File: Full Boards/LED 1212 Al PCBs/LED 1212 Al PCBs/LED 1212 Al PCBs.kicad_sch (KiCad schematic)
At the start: 3 parts

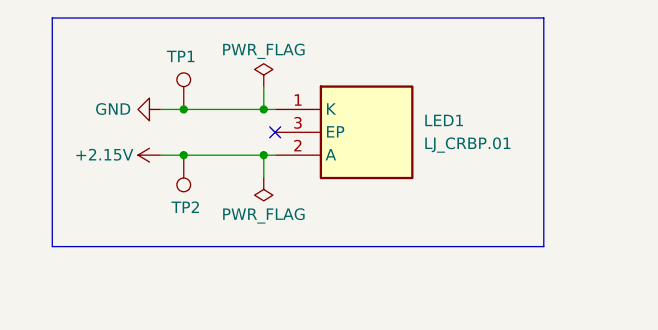
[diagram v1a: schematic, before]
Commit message: Sync'ed the USB-C PD PCB to the schematic.
Removed test points from the 1212 kicad schematic, as it was unused.

Signed-off-by: digimer <digital.mermaid@gmail.com>
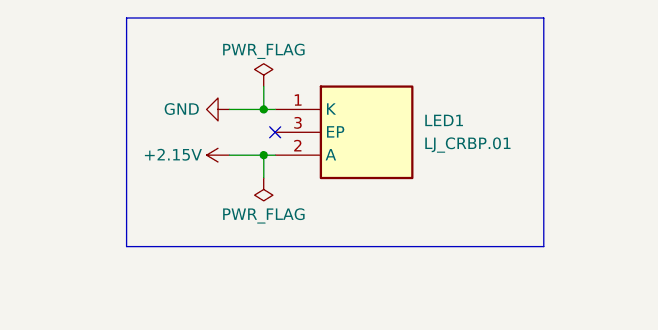
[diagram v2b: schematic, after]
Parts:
- removed TP1, TP2: TestPoint, TestPoint:TestPoint_Pad_4.0x4.0mm, symbol Connector:TestPoint
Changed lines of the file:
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@@
 	)
 	(rectangle
-		(start 92.075 72.39)
+		(start 100.33 72.39)
 		(end 146.685 97.79)
 		(stroke
@@
 	)
 	(junction
-		(at 106.68 87.63)
-		(diameter 0)
-		(color 0 0 0 0)
-	)
-	(junction
-		(at 106.68 82.55)
+		(at 115.57 87.63)
 		(diameter 0)
 		(color 0 0 0 0)
@@
 		(color 0 0 0 0)
 	)
-	(junction
-		(at 115.57 87.63)
-		(diameter 0)
-		(color 0 0 0 0)
-	)
 	(no_connect
 		(at 116.84 85.09)
@@
 	(wire
 		(pts
-			(xy 106.68 82.55) (xy 115.57 82.55)
+			(xy 111.76 82.55) (xy 115.57 82.55)
 		)
 		(stroke
@@
 	(wire
 		(pts
-			(xy 104.14 87.63) (xy 106.68 87.63)
-		)
-		(stroke
-			(width 0)
-			(type default)
-		)
-	)
-	(wire
-		(pts
-			(xy 104.14 82.55) (xy 106.68 82.55)
+			(xy 111.76 87.63) (xy 115.57 87.63)
 		)
 		(stroke
@@
 		(pts
 			(xy 115.57 82.55) (xy 116.84 82.55)
-		)
-		(stroke
-			(width 0)
-			(type default)
-		)
-	)
-	(wire
-		(pts
-			(xy 106.68 87.63) (xy 115.57 87.63)
 		)
 		(stroke
@@
 	)
 	(symbol
-		(lib_id "Connector:TestPoint")
-		(at 106.68 87.63 180)
-		(unit 1)
-		(body_style 1)
-		(exclude_from_sim no)
-		(in_bom yes)
-		(on_board yes)
-		(in_pos_files yes)
-		(dnp no)
-		(property "Reference" "TP2"
-			(at 106.934 93.472 0)
-			(show_name no)
-			(do_not_autoplace no)
-			(effects
-				(font
-					(size 1.27 1.27)
-				)
-			)
-		)
-		(property "Value" "TestPoint"
-			(at 104.14 89.6621 0)
-			(hide yes)
-			(show_name no)
-			(do_not_autoplace no)
-			(effects
-				(font
-					(size 1.27 1.27)
-				)
-				(justify left)
-			)
-		)
-		(property "Footprint" "TestPoint:TestPoint_Pad_4.0x4.0mm"
-			(at 101.6 87.63 0)
-			(hide yes)
-			(show_name no)
-			(do_not_autoplace no)
-			(effects
-				(font
-					(size 1.27 1.27)
-				)
-			)
-		)
-		(property "Datasheet" ""
-			(at 101.6 87.63 0)
-			(hide yes)
-			(show_name no)
-			(do_not_autoplace no)
-			(effects
-				(font
-					(size 1.27 1.27)
-				)
-			)
-		)
-		(property "Description" "test point"
-			(at 106.68 87.63 0)
-			(hide yes)
-			(show_name no)
-			(do_not_autoplace no)
-			(effects
-				(font
-					(size 1.27 1.27)
-				)
-			)
-		)
-		(pin "1"
-		)
-		(instances
-			(project "LED 1212 Al PCBs"
-				(path "/230f5e89-ed89-4016-bb7f-48da2e754b45"
-					(reference "TP2")
-					(unit 1)
-				)
-			)
-		)
-	)
-	(symbol
 		(lib_id "power:GND")
-		(at 104.14 82.55 270)
+		(at 111.76 82.55 270)
 		(unit 1)
 		(body_style 1)
@@
 		(dnp no)
 		(property "Reference" "#PWR02"
-			(at 97.79 82.55 0)
+			(at 105.41 82.55 0)
 			(hide yes)
 			(show_name no)
@@
 		)
 		(property "Value" "GND"
-			(at 100.838 82.55 90)
+			(at 108.458 82.55 90)
 			(show_name no)
 			(do_not_autoplace no)
@@
 		)
 		(property "Footprint" ""
-			(at 104.14 82.55 0)
+			(at 111.76 82.55 0)
 			(hide yes)
 			(show_name no)
@@
 		)
 		(property "Datasheet" ""
-			(at 104.14 82.55 0)
+			(at 111.76 82.55 0)
 			(hide yes)
 			(show_name no)
@@
 		)
 		(property "Description" "Power symbol creates a global label with name \"GND\" , ground"
-			(at 104.14 82.55 0)
+			(at 111.76 82.55 0)
 			(hide yes)
 			(show_name no)
@@
 	)
 	(symbol
-		(lib_id "Connector:TestPoint")
-		(at 106.68 82.55 0)
-		(unit 1)
-		(body_style 1)
-		(exclude_from_sim no)
-		(in_bom yes)
-		(on_board yes)
-		(in_pos_files yes)
-		(dnp no)
-		(property "Reference" "TP1"
-			(at 106.426 76.708 0)
-			(show_name no)
-			(do_not_autoplace no)
-			(effects
-				(font
-					(size 1.27 1.27)
-				)
-			)
-		)
-		(property "Value" "TestPoint"
-			(at 109.22 80.5179 0)
-			(hide yes)
-			(show_name no)
-			(do_not_autoplace no)
-			(effects
-				(font
-					(size 1.27 1.27)
-				)
-				(justify left)
-			)
-		)
-		(property "Footprint" "TestPoint:TestPoint_Pad_4.0x4.0mm"
-			(at 111.76 82.55 0)
-			(hide yes)
-			(show_name no)
-			(do_not_autoplace no)
-			(effects
-				(font
-					(size 1.27 1.27)
-				)
-			)
-		)
-		(property "Datasheet" ""
-			(at 111.76 82.55 0)
-			(hide yes)
-			(show_name no)
-			(do_not_autoplace no)
-			(effects
-				(font
-					(size 1.27 1.27)
-				)
-			)
-		)
-		(property "Description" "test point"
-			(at 106.68 82.55 0)
-			(hide yes)
-			(show_name no)
-			(do_not_autoplace no)
-			(effects
-				(font
-					(size 1.27 1.27)
-				)
-			)
-		)
-		(pin "1"
-		)
-		(instances
-			(project "LED 1212 Al PCBs"
-				(path "/230f5e89-ed89-4016-bb7f-48da2e754b45"
-					(reference "TP1")
-					(unit 1)
-				)
-			)
-		)
-	)
-	(symbol
 		(lib_id "power:+3.3V")
-		(at 104.14 87.63 90)
+		(at 111.76 87.63 90)
 		(unit 1)
 		(body_style 1)
@@
 		(dnp no)
 		(property "Reference" "#PWR01"
-			(at 107.95 87.63 0)
+			(at 115.57 87.63 0)
 			(hide yes)
 			(show_name no)
@@
 		)
 		(property "Value" "+2.15V"
-			(at 101.092 87.63 90)
+			(at 108.712 87.63 90)
 			(show_name no)
 			(do_not_autoplace no)
@@
 		)
 		(property "Footprint" ""
-			(at 104.14 87.63 0)
+			(at 111.76 87.63 0)
 			(hide yes)
 			(show_name no)
@@
 		)
 		(property "Datasheet" ""
-			(at 104.14 87.63 0)
+			(at 111.76 87.63 0)
 			(hide yes)
 			(show_name no)
@@
 		)
 		(property "Description" "Power symbol creates a global label with name \"+3.3V\""
-			(at 104.14 87.63 0)
-			(hide yes)
-			(show_name no)
+			(at 111.76 87.63 0)
+			(hide yes)
+			(show_name no)

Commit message: Updated LED 1212 PCB to add solder pads and wire solder pads (replacing what the test points were used for before).
Moved all .stp and .step files back one directory.

Signed-off-by: digimer <digital.mermaid@gmail.com>
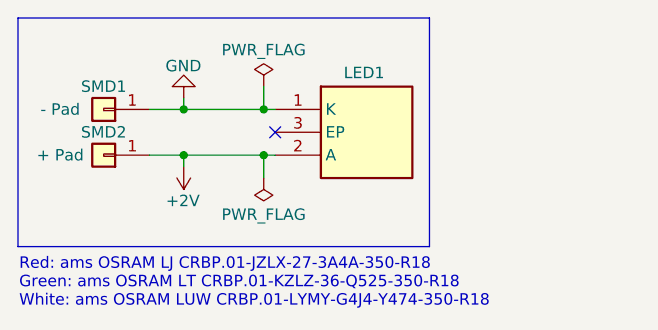
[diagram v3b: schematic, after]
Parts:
- added SMD1: - Pad, mr-stuff:SolderWirePad_1x01_SMD_4x4mm, symbol Connector_Generic:Conn_01x01
- added SMD2: + Pad, mr-stuff:SolderWirePad_1x01_SMD_4x4mm, symbol Connector_Generic:Conn_01x01
- LED1: Height 2.24 -> (none); Manufacturer_Name ams OSRAM -> (none); Manufacturer_Part_Number LJ CRBP.01-JZLX-27-3A4A -> (none); Mouser Part Number 720-LJCRBP01JZA9260 -> (none); Mouser Price/Stock https://www.mouser.co.uk/ProductDetail/ams-OSRAM/LJ-CRBP.01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 -> (none); Part - Green (none) -> ams OSRAM LT CRBP.01-KZLZ-36-Q525-350-R18; Part - Red (none) -> ams OSRAM LJ CRBP.01-JZLX-27-3A4A-350-R18; Part - White (none) -> ams OSRAM LUW CRBP.01-LYMY-G4J4-Y474-350-R18
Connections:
- net GND: now also SMD1.1 (Pin_1)
- net +2.15V renamed +2V
- net +2V: now also SMD2.1 (Pin_1)
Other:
- note added: "Red: ams OSRAM LJ CRBP.01-JZLX-27-3A4A-350-R18 Green: ams OSRAM LT CRBP.01-KZLZ-36-Q525-350-R18 White: ams OSRAM LUW CRBP.01-LYMY-G4J4-Y474-350-R18"
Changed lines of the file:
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@@
 	)
 	(rectangle
-		(start 100.33 72.39)
-		(end 146.685 97.79)
+		(start 88.265 72.39)
+		(end 133.985 97.79)
 		(stroke
 			(width 0)
@@
 		(fill
 			(type none)
+		)
+	)
+	(text "Red: ams OSRAM LJ CRBP.01-JZLX-27-3A4A-350-R18\nGreen: ams OSRAM LT CRBP.01-KZLZ-36-Q525-350-R18\nWhite: ams OSRAM LUW CRBP.01-LYMY-G4J4-Y474-350-R18"
+		(exclude_from_sim no)
+		(at 88.392 101.854 0)
+		(effects
+			(font
+				(size 1.27 1.27)
+			)
+			(justify left)
 		)
 	)
@@
 	)
 	(junction
+		(at 106.68 87.63)
+		(diameter 0)
+		(color 0 0 0 0)
+	)
+	(junction
+		(at 106.68 82.55)
+		(diameter 0)
+		(color 0 0 0 0)
+	)
+	(junction
 		(at 115.57 82.55)
 		(diameter 0)
@@
 	(wire
 		(pts
+			(xy 106.68 82.55) (xy 106.68 81.28)
+		)
+		(stroke
+			(width 0)
+			(type default)
+		)
+	)
+	(wire
+		(pts
 			(xy 115.57 87.63) (xy 115.57 90.17)
 		)
@@
 	(wire
 		(pts
+			(xy 102.87 82.55) (xy 106.68 82.55)
+		)
+		(stroke
+			(width 0)
+			(type default)
+		)
+	)
+	(wire
+		(pts
+			(xy 106.68 87.63) (xy 106.68 88.9)
+		)
+		(stroke
+			(width 0)
+			(type default)
+		)
+	)
+	(wire
+		(pts
+			(xy 106.68 82.55) (xy 115.57 82.55)
+		)
+		(stroke
+			(width 0)
+			(type default)
+		)
+	)
+	(wire
+		(pts
+			(xy 106.68 87.63) (xy 115.57 87.63)
+		)
+		(stroke
+			(width 0)
+			(type default)
+		)
+	)
+	(wire
+		(pts
 			(xy 115.57 80.01) (xy 115.57 82.55)
 		)
@@
 	(wire
 		(pts
-			(xy 111.76 82.55) (xy 115.57 82.55)
-		)
-		(stroke
-			(width 0)
-			(type default)
-		)
-	)
-	(wire
-		(pts
-			(xy 111.76 87.63) (xy 115.57 87.63)
+			(xy 102.87 87.63) (xy 106.68 87.63)
 		)
 		(stroke
@@
 	)
 	(symbol
+		(lib_id "Connector_Generic:Conn_01x01")
+		(at 97.79 82.55 180)
+		(unit 1)
+		(body_style 1)
+		(exclude_from_sim no)
+		(in_bom yes)
+		(on_board yes)
+		(in_pos_files yes)
+		(dnp no)
+		(property "Reference" "SMD1"
+			(at 97.79 80.01 0)
+			(show_name no)
+			(do_not_autoplace no)
+			(effects
+				(font
+					(size 1.27 1.27)
+				)
+			)
+		)
+		(property "Value" "- Pad"
+			(at 92.964 82.55 0)
+			(show_name no)
+			(do_not_autoplace no)
+			(effects
+				(font
+					(size 1.27 1.27)
+				)
+			)
+		)
+		(property "Footprint" "mr-stuff:SolderWirePad_1x01_SMD_4x4mm"
+			(at 97.79 82.55 0)
+			(hide yes)
+			(show_name no)
+			(do_not_autoplace no)
+			(effects
+				(font
+					(size 1.27 1.27)
+				)
+			)
+		)
+		(property "Datasheet" ""
+			(at 97.79 82.55 0)
+			(hide yes)
+			(show_name no)
+			(do_not_autoplace no)
+			(effects
+				(font
+					(size 1.27 1.27)
+				)
+			)
+		)
+		(property "Description" "4x4mm SMD pad"
+			(at 97.79 82.55 0)
+			(hide yes)
+			(show_name no)
+			(do_not_autoplace no)
+			(effects
+				(font
+					(size 1.27 1.27)
+				)
+			)
+		)
+		(pin "1"
+		)
+		(instances
+			(project "LED 1212 Al PCBs"
+				(path "/230f5e89-ed89-4016-bb7f-48da2e754b45"
+					(reference "SMD1")
+					(unit 1)
+				)
+			)
+		)
+	)
+	(symbol
 		(lib_id "power:GND")
-		(at 111.76 82.55 270)
+		(at 106.68 81.28 180)
 		(unit 1)
 		(body_style 1)
@@
 		(dnp no)
 		(property "Reference" "#PWR02"
-			(at 105.41 82.55 0)
+			(at 106.68 74.93 0)
 			(hide yes)
 			(show_name no)
@@
 		)
 		(property "Value" "GND"
-			(at 108.458 82.55 90)
+			(at 104.648 77.724 0)
 			(show_name no)
 			(do_not_autoplace no)
@@
 		)
 		(property "Footprint" ""
-			(at 111.76 82.55 0)
+			(at 106.68 81.28 0)
 			(hide yes)
 			(show_name no)
@@
 		)
 		(property "Datasheet" ""
-			(at 111.76 82.55 0)
+			(at 106.68 81.28 0)
 			(hide yes)
 			(show_name no)
@@
 		)
 		(property "Description" "Power symbol creates a global label with name \"GND\" , ground"
-			(at 111.76 82.55 0)
+			(at 106.68 81.28 0)
 			(hide yes)
 			(show_name no)
@@
 		(in_pos_files yes)
 		(dnp no)
-		(fields_autoplaced yes)
 		(property "Reference" "LED1"
-			(at 133.35 83.8199 0)
+			(at 124.46 78.486 0)
 			(show_name no)
 			(do_not_autoplace no)
@@
 		)
 		(property "Value" "LJ_CRBP.01"
-			(at 133.35 86.3599 0)
+			(at 122.174 92.202 0)
+			(hide yes)
 			(show_name no)
 			(do_not_autoplace no)
@@
 			)
 		)
-		(property "Height" "2.24"
+		(property "Part - Red" "ams OSRAM LJ CRBP.01-JZLX-27-3A4A-350-R18"
 			(at 143.51 480.01 0)
 			(hide yes)
@@
 			)
 		)
-		(property "Manufacturer_Name" "ams OSRAM"
-			(at 143.51 580.01 0)
-			(hide yes)
-			(show_name no)
-			(do_not_autoplace no)
-			(effects
-				(font
-					(size 1.27 1.27)
-				)
-				(justify left top)
-			)
-		)
-		(property "Manufacturer_Part_Number" "LJ CRBP.01-JZLX-27-3A4A"
-			(at 143.51 680.01 0)
-			(hide yes)
-			(show_name no)
-			(do_not_autoplace no)
-			(effects
-				(font
-					(size 1.27 1.27)
-				)
-				(justify left top)
-			)
-		)
-		(property "Mouser Part Number" "720-LJCRBP01JZA9260"
-			(at 143.51 780.01 0)
-			(hide yes)
-			(show_name no)
-			(do_not_autoplace no)
-			(effects
-				(font
-					(size 1.27 1.27)
-				)
-				(justify left top)
-			)
-		)
-		(property "Mouser Price/Stock" "https://www.mouser.co.uk/ProductDetail/ams-OSRAM/LJ-CRBP.01-JZLX-27-3A4A?qs=vvQtp7zwQdO%252B1A3QlQcixg%3D%3D"
-			(at 143.51 880.01 0)
-			(hide yes)
-			(show_name no)
-			(do_not_autoplace no)
-			(effects
-				(font
-					(size 1.27 1.27)
-				)
-				(justify left top)
-			)
-		)
-		(property "Arrow Part Number" ""
-			(at 143.51 980.01 0)
-			(hide yes)
-			(show_name no)
-			(do_not_autoplace no)
-			(effects
-				(font
-					(size 1.27 1.27)
-				)
-				(justify left top)
-			)
-		)
-		(property "Arrow Price/Stock" ""
-			(at 143.51 1080.01 0)
-			(hide yes)
-			(show_name no)
-			(do_not_autoplace no)
-			(effects
-				(font
-					(size 1.27 1.27)
-				)
-				(justify left top)
+		(property "Part - Green" "ams OSRAM LT CRBP.01-KZLZ-36-Q525-350-R18"
+			(at 127 85.09 0)
+			(hide yes)
+			(show_name no)
+			(do_not_autoplace no)
+			(effects
+				(font
+					(size 1.27 1.27)
+				)
+			)
+		)
+		(property "Part - White" "ams OSRAM LUW CRBP.01-LYMY-G4J4-Y474-350-R18"
+			(at 127 85.09 0)
+			(hide yes)
+			(show_name no)
+			(do_not_autoplace no)
+			(effects
+				(font
+					(size 1.27 1.27)
+				)
 			)
 		)
@@
 	)
 	(symbol
+		(lib_id "Connector_Generic:Conn_01x01")
+		(at 97.79 87.63 180)
+		(unit 1)
+		(body_style 1)
+		(exclude_from_sim no)
+		(in_bom yes)
+		(on_board yes)
+		(in_pos_files yes)
+		(dnp no)
+		(property "Reference" "SMD2"
+			(at 97.79 85.09 0)
+			(show_name no)
+			(do_not_autoplace no)
+			(effects
+				(font
+					(size 1.27 1.27)
+				)
+			)
+		)
+		(property "Value" "+ Pad"
+			(at 92.964 87.63 0)
+			(show_name no)
+			(do_not_autoplace no)
+			(effects
+				(font
+					(size 1.27 1.27)
+				)
+			)
+		)
+		(property "Footprint" "mr-stuff:SolderWirePad_1x01_SMD_4x4mm"
+			(at 97.79 87.63 0)
+			(hide yes)
+			(show_name no)
+			(do_not_autoplace no)
+			(effects
+				(font
+					(size 1.27 1.27)
+				)
+			)
+		)
+		(property "Datasheet" ""
+			(at 97.79 87.63 0)
+			(hide yes)
+			(show_name no)
+			(do_not_autoplace no)
+			(effects
+				(font
+					(size 1.27 1.27)
+				)
+			)
+		)
+		(property "Description" "4x4mm SMD pad"
+			(at 97.79 87.63 0)
+			(hide yes)
+			(show_name no)
+			(do_not_autoplace no)
+			(effects
+				(font
+					(size 1.27 1.27)
+				)
+			)
+		)
+		(pin "1"
+		)
+		(instances
+			(project "LED 1212 Al PCBs"
+				(path "/230f5e89-ed89-4016-bb7f-48da2e754b45"
+					(reference "SMD2")
+					(unit 1)
+				)
+			)
+		)
+	)
+	(symbol
 		(lib_id "power:+3.3V")
-		(at 111.76 87.63 90)
+		(at 106.68 88.9 180)
 		(unit 1)
 		(body_style 1)
@@
 		(dnp no)
 		(property "Reference" "#PWR01"
-			(at 115.57 87.63 0)
-			(hide yes)
-			(show_name no)
-			(do_not_autoplace no)
-			(effects
-				(font
-					(size 1.27 1.27)
-				)
-			)
-		)
-		(property "Value" "+2.15V"
-			(at 108.712 87.63 90)
+			(at 106.68 85.09 0)
+			(hide yes)
+			(show_name no)
+			(do_not_autoplace no)
+			(effects
+				(font
+					(size 1.27 1.27)
+				)
+			)
+		)
+		(property "Value" "+2V"
+			(at 108.458 92.71 0)
 			(show_name no)
 			(do_not_autoplace no)
@@
 		)
 		(property "Footprint" ""
-			(at 111.76 87.63 0)
+			(at 106.68 88.9 0)
 			(hide yes)
 			(show_name no)
@@
 		)
 		(property "Datasheet" ""
-			(at 111.76 87.63 0)
+			(at 106.68 88.9 0)
 			(hide yes)
 			(show_name no)
@@
 		)
 		(property "Description" "Power symbol creates a global label with name \"+3.3V\""
-			(at 111.76 87.63 0)
-			(hide yes)
-			(show_name no)
+			(at 106.68 88.9 0)
+			(hide yes)
+			(show_name no)
